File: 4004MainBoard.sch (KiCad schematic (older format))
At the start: 101 parts, among them J1 BUS, J2 P0 RAM1, J3 CMRAM RAM2, J4 P0 RAM2, J5 DC 5V, Q1 2SA1162GR, Q10 2SC2712GR, Q11 2SA1162GR, Q2 2SC2712GR, Q3 2SA1162GR, Q4 2SC2712GR, Q5 2SA1162GR, Q6 2SA1162GR, Q7 2SA1162GR, Q8 2SA1162GR, Q9 2SC2712GR, SW1 TEST, SW2 RESET, SW3 POWER, U1 74HC08, U2 74HC161, U3 PST600, U4 Intel4004, U5 LT1931A, U6 74LS540, U7 Intel4002-1, U8 Intel4002-1, U9 LT1763, Y1 DLO555MB

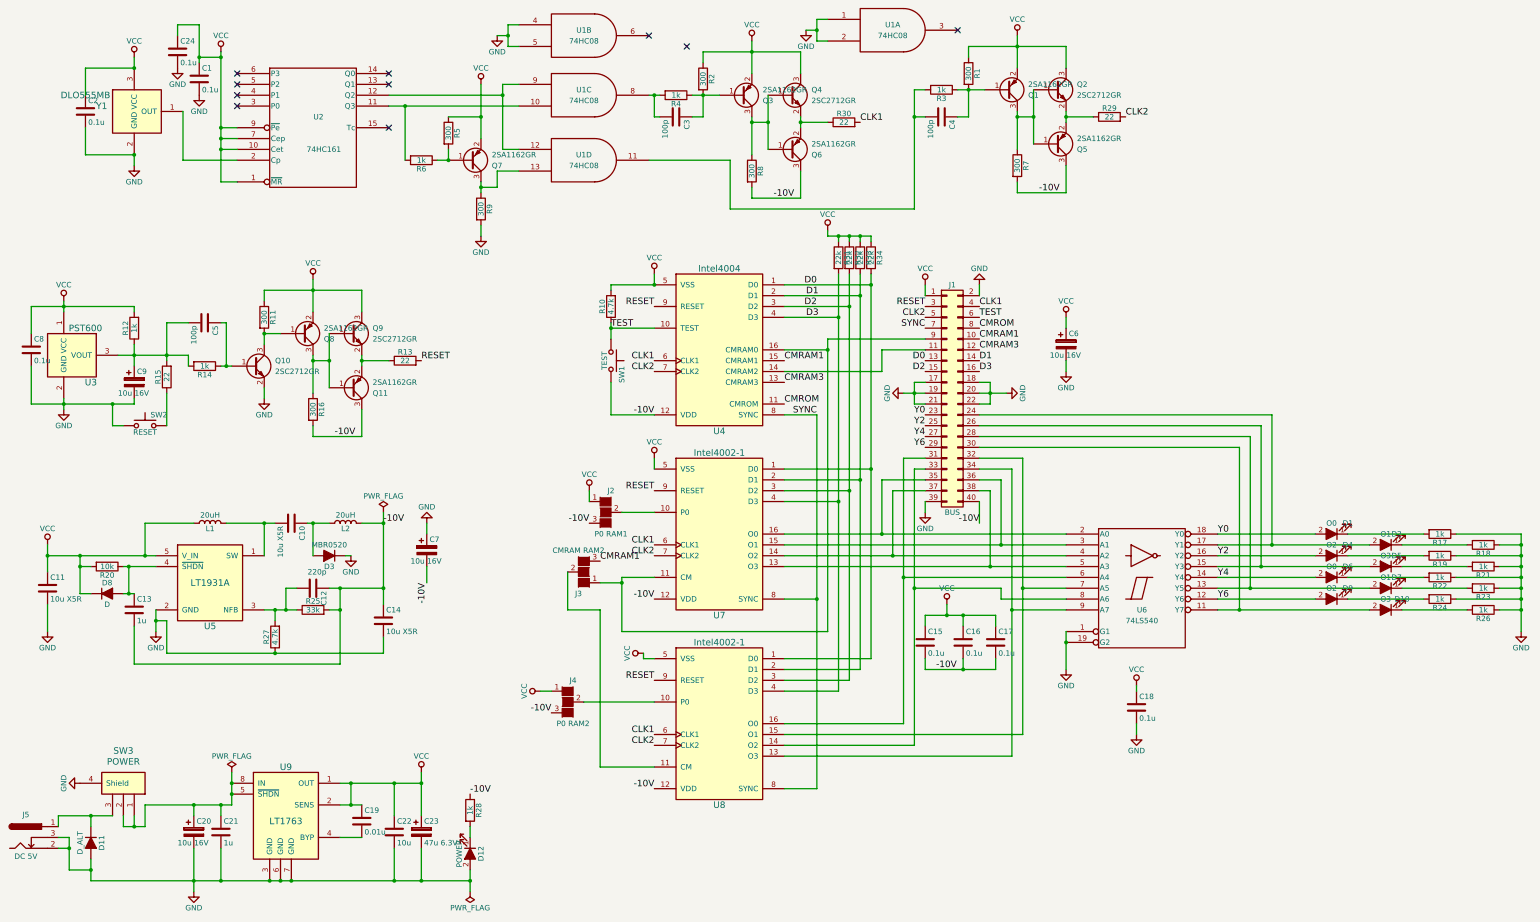
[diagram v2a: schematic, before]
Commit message: 回路修正 シルク修正
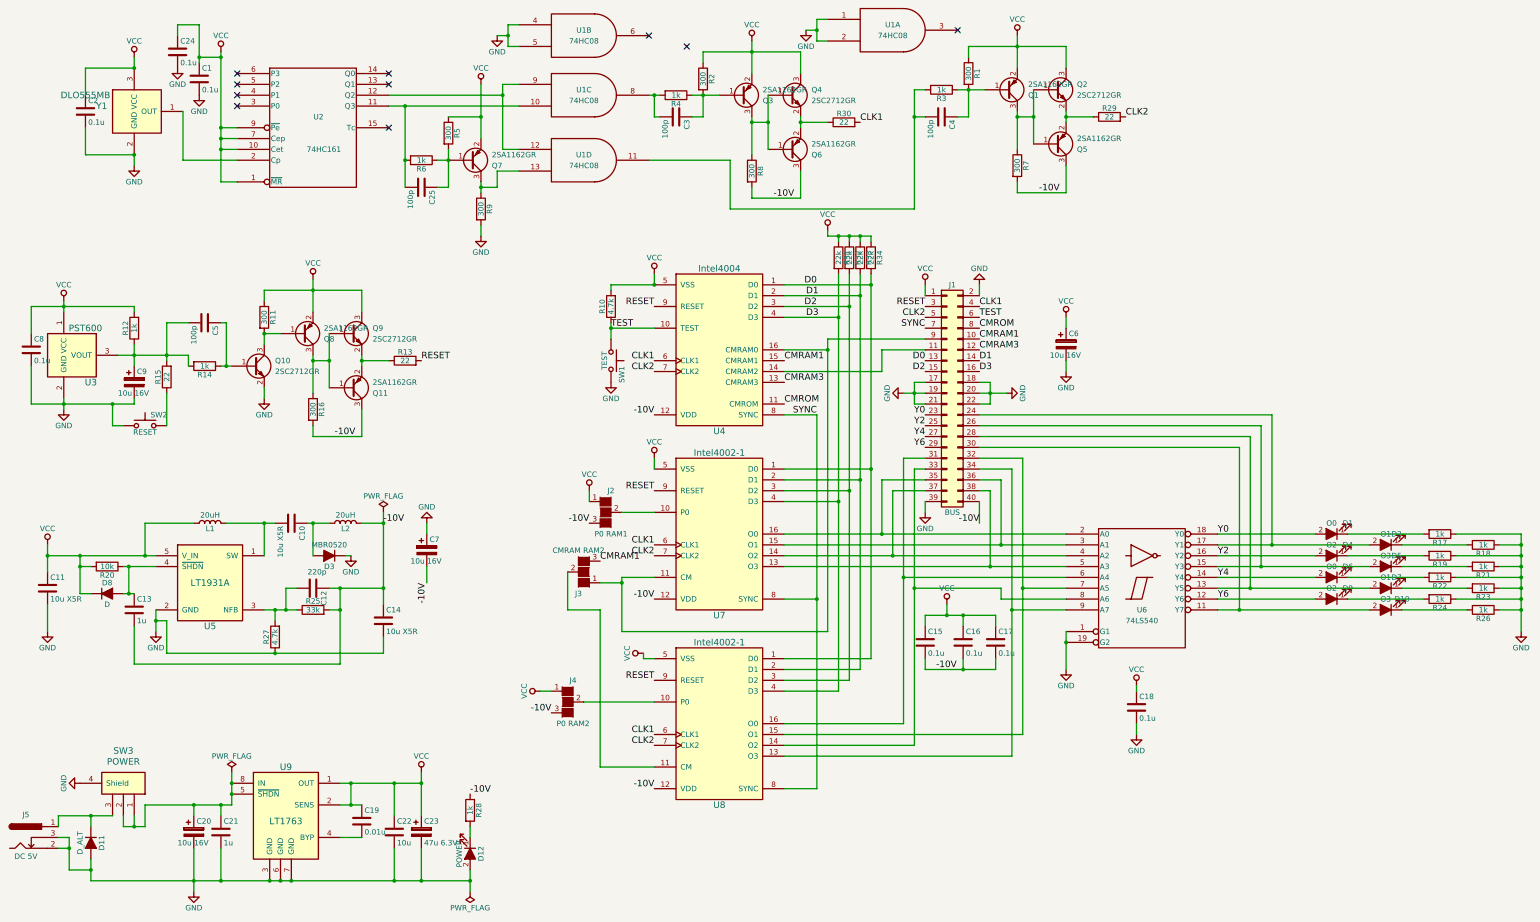
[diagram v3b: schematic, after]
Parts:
- added C25: 100p, Capacitors_SMD:C_0603_HandSoldering, symbol C
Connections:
- net -10V: no longer SW1.2
- net GND: now also SW1.2
- net at R6.2, U1.10, U2.11 (Q3): now also C25.2
- net at Q7.1 (B), R5.2, R6.1: now also C25.1
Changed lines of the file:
@@
 	1    0    0    -1
 $EndComp
-Text Label 6900 4800 2    60   ~ 0
--10V
 Text Label 6900 4300 2    60   ~ 0
 CLK1
@@
 	2200 8600 2200 8400
 Wire Wire Line
-	2200 8400 3000 8400
-Wire Wire Line
-	3000 8400 3000 8100
+	3000 8400 2200 8400
+Wire Wire Line
+	3000 8100 3000 8400
 Connection ~ 2100 8600
 Connection ~ 3000 8300
@@
 	4900 2450 5000 2450
 Wire Wire Line
-	5000 2450 5000 2350
+	5000 2350 5000 2700
 Connection ~ 5000 2450
 Wire Wire Line
@@
 	4450 1850 5500 1850
 Wire Wire Line
-	4600 2450 4600 1950
+	4600 1950 4600 2700
 Connection ~ 4600 1950
 Wire Wire Line
@@
 	7600 2450 7600 2900
 Wire Wire Line
-	7600 2900 9300 2900
-Wire Wire Line
-	9300 2900 9300 1800
+	9300 2900 7600 2900
+Wire Wire Line
+	9300 1800 9300 2900
 Wire Wire Line
 	9300 1800 9400 1800
@@
 	8500 4100 8500 6800
 Wire Wire Line
-	8500 6800 6600 6800
-Wire Wire Line
-	6600 6800 6600 6300
+	6600 6800 8500 6800
+Wire Wire Line
+	6600 6300 6600 6800
 Wire Wire Line
 	6600 6300 6900 6300
@@
 	8600 5600 8100 5600
 Wire Wire Line
-	8100 5500 8700 5500
+	8700 5500 8100 5500
 Wire Wire Line
 	8700 3500 8700 7250
@@
 	8700 3800 8100 3800
 Wire Wire Line
-	8100 5400 8800 5400
+	8800 5400 8100 5400
 Wire Wire Line
 	8800 3500 8800 7150
@@
 	8800 3700 8100 3700
 Wire Wire Line
-	8100 5300 8900 5300
+	8900 5300 8100 5300
 Wire Wire Line
 	8900 3500 8900 7050
@@
 Wire Wire Line
 	6600 5700 6900 5700
-Wire Wire Line
-	6900 4800 6500 4800
-Wire Wire Line
-	6500 4800 6500 4500
 Wire Wire Line
 	6500 3950 6500 4100
@@
 Connection ~ 8800 3700
 Connection ~ 8900 3600
+$Comp
+L C C25
+U 1 1 5AF7EC6C
+P 4750 2700
+F 0 "C25" H 4775 2800 50  0000 L CNN
+F 1 "100p" H 4775 2600 50  0000 L CNN
+F 2 "Capacitors_SMD:C_0603_HandSoldering" H 4788 2550 50  0001 C CNN
+F 3 "" H 4750 2700 50  0001 C CNN
+	1    4750 2700
+	0    1    1    0
+$EndComp
+Connection ~ 4600 2450
+Wire Wire Line
+	5000 2700 4900 2700
+Text Label 6900 4800 2    60   ~ 0
+-10V
+$Comp
+L GND #PWR045
+U 1 1 5AF7FECE
+P 6500 4500
+F 0 "#PWR045" H 6500 4250 50  0001 C CNN
+F 1 "GND" H 6500 4350 50  0000 C CNN
+F 2 "" H 6500 4500 50  0001 C CNN
+F 3 "" H 6500 4500 50  0001 C CNN
+	1    6500 4500
+	1    0    0    -1
+$EndComp
 $EndSCHEMATC

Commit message: 電源電圧調整 基板修正
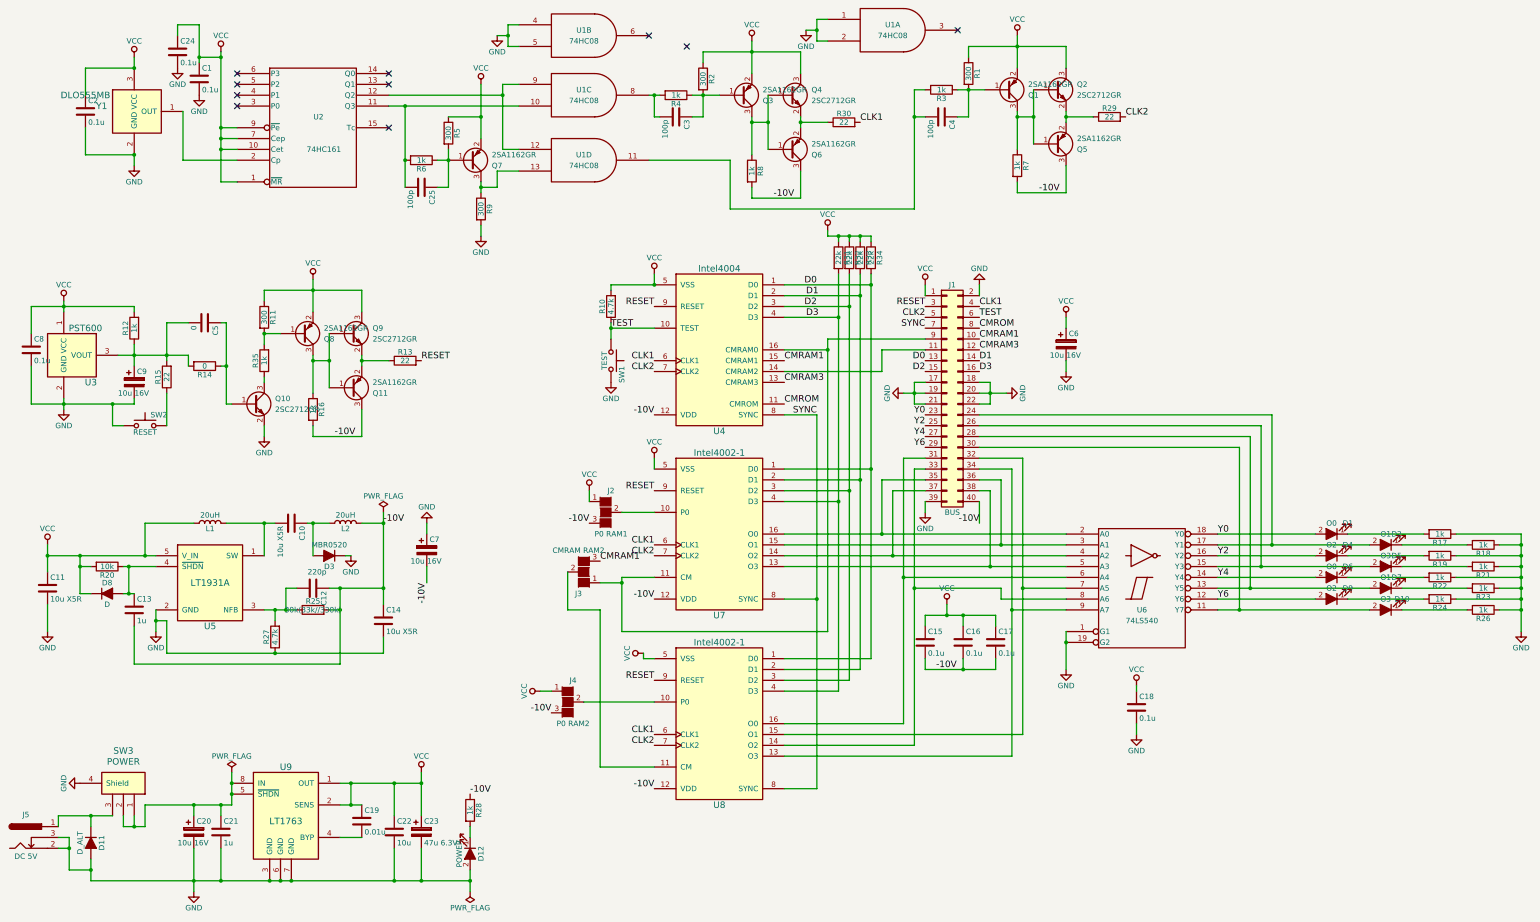
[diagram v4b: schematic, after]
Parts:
- added R35: 1k, Resistors_SMD:R_0603_HandSoldering, symbol R
- C5: value 100p -> 0
- R14: value 1k -> 0
- R16, R7, R8: value 300 -> 1k
- R25: value 33k -> 30k(33k//330k)
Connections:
- net at Q8.1 (B), R11.2: now also R35.2; no longer Q10.3 (C)
- new net: Q10.3 (C), R35.1
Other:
- moved on the sheet: Q10
